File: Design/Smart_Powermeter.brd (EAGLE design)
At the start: 80 x 70 mm, 48 parts, among them J1 AUDIO_JACK_TRRSSMD_RA, J2 AUDIO_JACK_TRRSSMD_RA, J3 AUDIO_JACK_TRRSSMD_RA, J4 AUDIO_JACK_TRRSSMD_RA, J5 AUDIO_JACK_TRRSSMD_RA, J6 AUDIO_JACK_TRRSSMD_RA, J7 AUDIO_JACK_TRRSSMD_RA, J8 AUDIO_JACK_TRRSSMD_RA

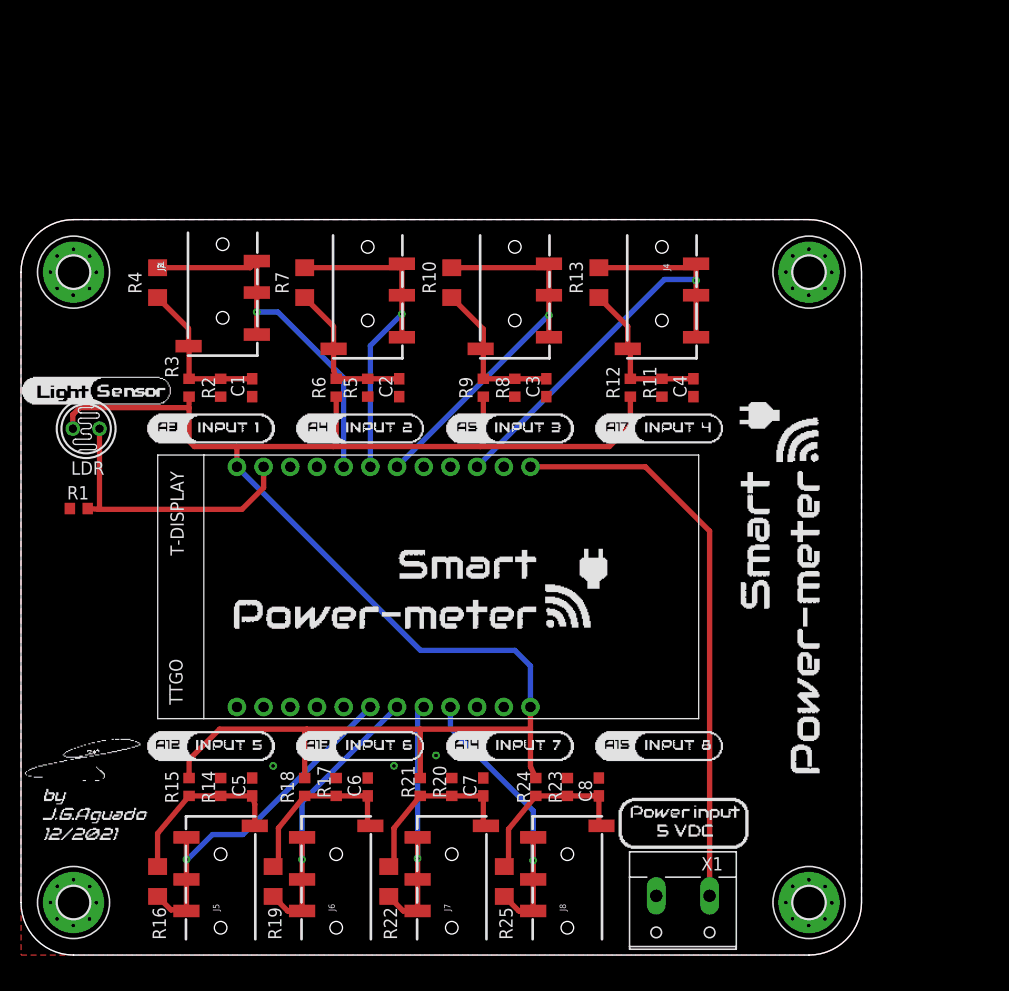
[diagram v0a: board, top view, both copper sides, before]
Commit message: Updated design files fixing Release 1 bugs
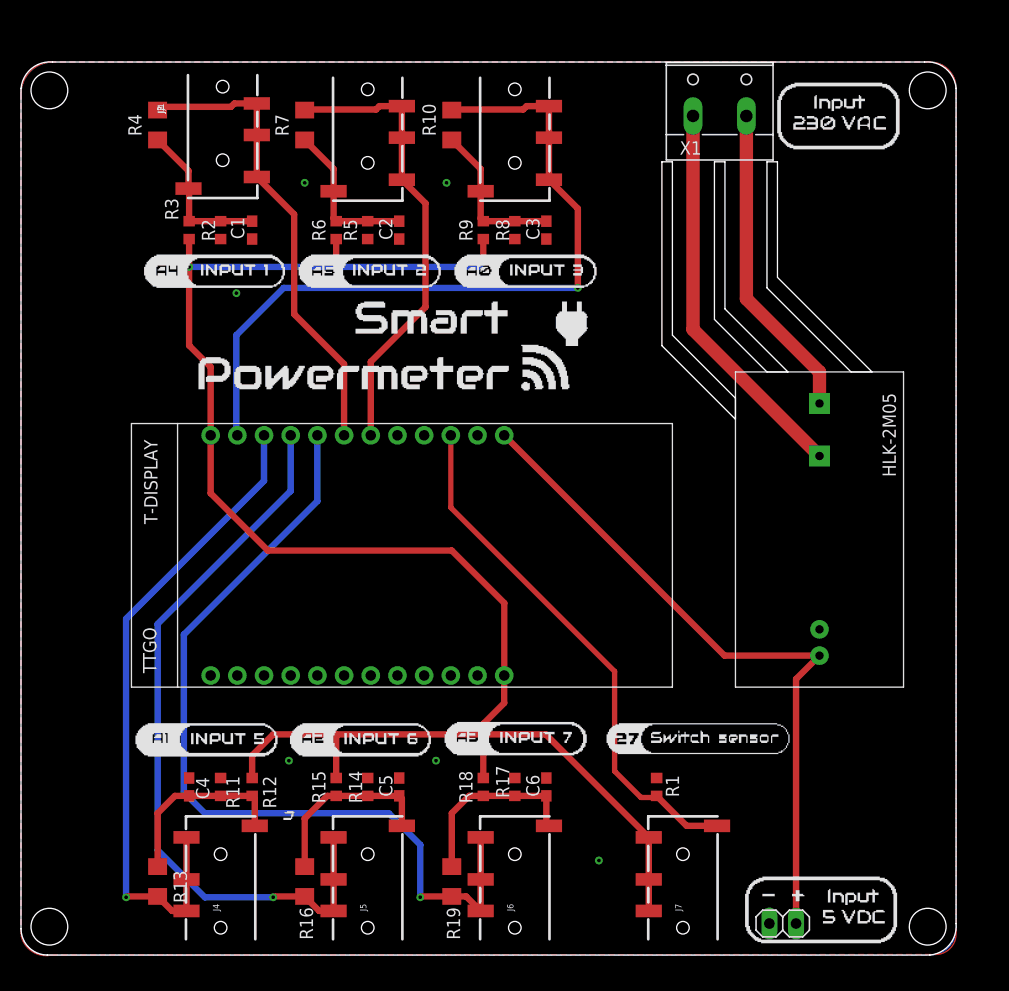
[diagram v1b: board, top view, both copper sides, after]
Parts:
- removed C7, C8: 10u, rcl:C0603
- removed H1, H2, H3, H4: MOUNT-PAD-ROUND3.0, holes:3,0-PAD
- removed J8: AUDIO_JACK_TRRSSMD_RA, SparkFun-Connectors:AUDIO_JACK_3.5MM_TRRS_SMD_RA
- removed LDR: VT20N1, photo-elements:TO46-VT200
- removed R20, R21, R23, R24: 10k, rcl:R0603
- removed R22, R25: 22, rcl:R1206
- added JP1: (no value), pinhead:1X02
- added U$2: HLK-2M05, SpaceDIY_modules:HLK-2M05
- moved J4 79.9 mm to (19.0, 1.00), turned to 90 degrees
- moved X1 75.6 mm to (66.5, 80.5), turned to 0 degrees
- moved R13 70.8 mm to (13.0, 7.00), turned to 270 degrees
- moved C4 61.2 mm to (16.0, 16.0), turned to 90 degrees
- moved R1 61.1 mm to (60.5, 16.0), turned to 270 degrees
- moved R11 56.6 mm to (19.0, 16.0), turned to 270 degrees
- moved R12 52.3 mm to (22.0, 16.0), turned to 90 degrees
- moved J7 22.0 mm to (63.0, 1.00)
- moved C6 17.0 mm to (50.0, 16.0)
- moved J6 17.0 mm to (47.0, 1.00)
- moved R17 17.0 mm to (47.0, 16.0)
- moved R18 17.0 mm to (44.0, 16.0)
- moved R19 17.0 mm to (41.0, 7.00)
- moved C1 15.0 mm to (22.0, 69.0)
- moved C2 15.0 mm to (36.0, 69.0)
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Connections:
- removed net LIGHT: LDR.2, R1.2, U$1.SVP-G36-A0
- removed net M7: J7.RING1, J7.RING2, J7.TIP, R22.2, U$1.13-G13-A14
- removed net M8: J8.RING1, J8.RING2, J8.TIP, R25.2, U$1.12-G12-A15
- removed net VG7: C7.1, J7.EARTH, R20.2, R21.1, R22.1
- removed net VG8: C8.1, J8.EARTH, R23.2, R24.1, R25.1
- new net N$1: U$2.AC1, X1.2
- new net N$2: U$2.AC2, X1.1
- new net PB: J7.EARTH, R1.2, U$1.27-G27-A17
- net 3.3V: now also J7.RING1, J7.RING2, J7.TIP; no longer LDR.1, R21.2, R24.2
- net 5V: now also JP1.2, U$2.+V0; no longer X1.1
- net GND: now also JP1.1, U$2.-V0; no longer C7.2, C8.2, H1.B3,0, H2.B3,0, H3.B3,0, H4.B3,0, R20.1, R23.1, X1.2
- net M1: now also U$1.32-G32-A4; no longer U$1.SVN-G39-A3
- net M2: now also U$1.33-G33-A5; no longer U$1.32-G32-A4
- net M3: now also U$1.SVP-G36-A0; no longer U$1.33-G33-A5
- net M4: now also U$1.37-G37; no longer U$1.27-G27-A17
- net M5: now also U$1.38-G38; no longer U$1.2-G2-A12
- net M6: now also U$1.SVN-G39-A3; no longer U$1.15-G15-A13
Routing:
- net M6: track 28.6 -> 82.2 mm
- net PB: track 0.00 -> 50.5 mm
- net N$2: track 0.00 -> 37.4 mm
- net M5: track 33.8 -> 70.9 mm
- net M3: track 36.8 -> 71.8 mm
- net N$1: track 0.00 -> 30.2 mm
- net M8: track 28.2 -> 0.00 mm, vias 1 -> 0
- net LIGHT: track 27.3 -> 0.00 mm
- net M7: track 25.0 -> 0.00 mm, vias 1 -> 0
- net M4: track 44.7 -> 62.8 mm
- net VG8: track 17.2 -> 0.00 mm
- net VG7: track 16.9 -> 0.00 mm
- net M2: track 32.2 -> 43.8 mm, vias 1 -> 0
- net 5V: track 54.3 -> 65.1 mm
- net M1: track 36.0 -> 44.7 mm, vias 1 -> 0
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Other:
- board size 80 x 70 mm -> 89 x 85 mm

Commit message: Resize dimensions to fit in the 92x87 enclosure
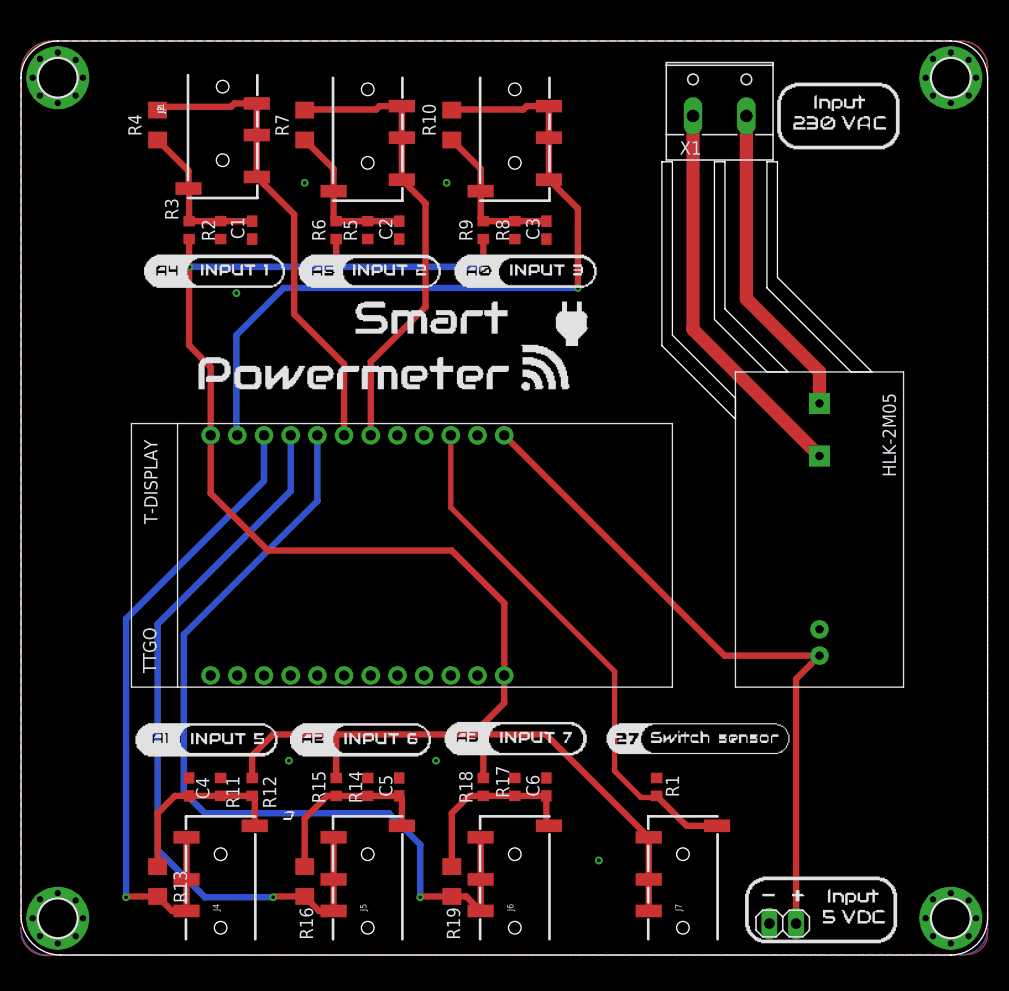
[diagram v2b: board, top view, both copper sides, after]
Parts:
- added FRAME1: (no value), SpaceDIY_symbols:92X87
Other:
- board size 89 x 85 mm -> 92 x 87 mm
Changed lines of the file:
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@@
 <setting verticaltext="up"/>
 </settings>
-<grid distance="0.1177" unitdist="mm" unit="mm" style="lines" multiple="1" display="yes" altdistance="5" altunitdist="mil" altunit="mil"/>
+<grid distance="1" unitdist="mm" unit="mm" style="lines" multiple="1" display="yes" altdistance="5" altunitdist="mil" altunit="mil"/>
 <layers>
 <layer number="1" name="Top" color="4" fill="1" visible="yes" active="yes"/>
@@
 <layer number="47" name="Measures" color="7" fill="1" visible="no" active="yes"/>
 <layer number="48" name="Document" color="7" fill="1" visible="no" active="yes"/>
-<layer number="49" name="Reference" color="7" fill="1" visible="no" active="yes"/>
+<layer number="49" name="Reference" color="7" fill="1" visible="yes" active="yes"/>
 <layer number="50" name="dxf" color="7" fill="1" visible="no" active="no"/>
 <layer number="51" name="tDocu" color="7" fill="1" visible="yes" active="yes"/>
@@
 <board>
 <plain>
-<wire x1="0" y1="2.5" x2="2.5" y2="0" width="0" layer="20" curve="90"/>
-<wire x1="2.5" y1="0" x2="86.5" y2="0" width="0" layer="20"/>
-<wire x1="86.5" y1="0" x2="89" y2="3" width="0" layer="20" curve="90"/>
-<wire x1="89" y1="3" x2="89" y2="82.5" width="0" layer="20"/>
-<wire x1="89" y1="82.5" x2="86" y2="85" width="0" layer="20" curve="90"/>
-<wire x1="86" y1="85" x2="3" y2="85" width="0" layer="20"/>
-<wire x1="3" y1="85" x2="0" y2="82.5" width="0" layer="20" curve="90"/>
-<wire x1="0" y1="82.5" x2="0" y2="2.5" width="0" layer="20"/>
 <rectangle x1="24.9691" y1="12.8547" x2="25.7097" y2="12.9605" layer="25"/>
 <rectangle x1="24.9691" y1="12.9605" x2="25.8155" y2="13.0663" layer="25"/>
@@
 <rectangle x1="25.0749" y1="13.4895" x2="26.0271" y2="13.5953" layer="25"/>
 <rectangle x1="25.2865" y1="13.5953" x2="25.9213" y2="13.7011" layer="25"/>
-<hole x="2.7" y="2.7" drill="3.5"/>
-<hole x="2.7" y="82.3" drill="3.5"/>
-<hole x="86.3" y="82.3" drill="3.5"/>
-<hole x="86.3" y="2.7" drill="3.5"/>
 <polygon width="0.6096" layer="41">
 <vertex x="60" y="85"/>
@@
 <attribute name="VALUE" x="69.96" y="-0.175" size="1.27" layer="27"/>
 </element>
+<element name="FRAME1" library="SpaceDIY_symbols" package="92X87" value="" x="0" y="0" smashed="yes"/>
 </elements>
 <signals>
@@
 <contactref element="U$1" pad="GND_2"/>
 <polygon width="0.508" layer="1">
-<vertex x="3" y="85" curve="90"/>
-<vertex x="0" y="82"/>
+<vertex x="3" y="87" curve="90"/>
+<vertex x="0" y="84"/>
 <vertex x="0" y="1.861153125" curve="90"/>
-<vertex x="2.91329375" y="0"/>
-<vertex x="87.05454375" y="0.05454375" curve="90"/>
-<vertex x="89" y="2"/>
-<vertex x="89" y="82.5" curve="90"/>
-<vertex x="86.5" y="85"/>
+<vertex x="2.916334375" y="-0.00194375"/>
+<vertex x="90.05454375" y="0.05454375" curve="90"/>
+<vertex x="92" y="2"/>
+<vertex x="92" y="84.5" curve="90"/>
+<vertex x="89.5" y="87"/>
 </polygon>
 <polygon width="0.508" layer="16">
-<vertex x="3" y="85" curve="90"/>
-<vertex x="0" y="82"/>
+<vertex x="3" y="87" curve="90"/>
+<vertex x="0" y="84"/>
 <vertex x="0" y="2.5" curve="90"/>
 <vertex x="2.5" y="0"/>
-<vertex x="86.5" y="0" curve="90"/>
-<vertex x="89" y="2.5"/>
-<vertex x="89" y="82.5" curve="90"/>
-<vertex x="86.5" y="85"/>
+<vertex x="89.5" y="0" curve="90"/>
+<vertex x="92" y="2.5"/>
+<vertex x="92" y="84.5" curve="90"/>
+<vertex x="89.5" y="87"/>
 </polygon>
 <contactref element="U$2" pad="-V0"/>

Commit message: Added design files of V2
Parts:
- removed JP1: (no value), pinhead:1X02
- added C10, C12, C16, C20, C8: 10uF, rcl:C0603
- added C11, C15, C21: 0.1uF, rcl:C0603
- added C13, C14, C17, C18, C19, C25, C27, C28, C9: 1uF, rcl:C0603
- added C26, C7: 4.7uF, rcl:C0603
- added D1, D2, D3: SS14, SpaceDIY_semiconductors:SMA-DIODE
- added DISP1: DISP_LCD_GENERIC_SPI_1.69_WRAPUNDER, adafruit_display:TFT_1.69IN_240X280_12P
- added IC1: AMS1117-3.3, SparkFun-IC-Power:SOT223
- added IC3: ESP32-S2-MINI-1-N4R2, SpaceDIY_modules:ESP32S2MINI1N4R2
- added IC5: BMP280, SamacSys_Parts:8-PIN-METAL-LID-LGA
- added J8: USB-C, SparkFun-Connectors:USB-C-16P-4LAYER-ISOLATED
- added L3: 10uH, microbuilder:INDUCTOR_4X4MM_NR401
- added Q1: IRLML0100, Parts:SOT23-3
- added Q2: 2N7002, SparkFun-DiscreteSemi:SOT23-3
- added R20, R21, R22, R26, R28, R29: 10k, rcl:R0603
- added R23, R24: 4.7k, rcl:R0603
- added R25: 10K, rcl:R0603
- added R27: 10, rcl:R0603
- added R36, R37: 5.1k, rcl:R0603
- added S1: Flash, SpaceDIY_electromechanical:TACTILE_SWITCH_SMD_5.2MM
- added S2: Reset, SpaceDIY_electromechanical:TACTILE_SWITCH_SMD_5.2MM
- added SJ1, SJ2: SOLDERJUMPERROUND, SparkFun-Retired:SJ_ROUND
- H1: value (none) -> 92X84
- J7: value AUDIO_JACK_TRRSSMD_RA -> (none); device SparkFun-Connectors:AUDIO_JACK_3.5MM_TRRS_SMD_RA -> SparkFun-Connectors:1X04
- R1: value 10k -> 0.47
- U$1: value TTGO-T-DISPLAYFRAME -> E-PAPER-FPC_2; device TTGO-TDisplay:TTGO-T-DISPLAY-OL -> SpaceDIY_connectors:FPC-05FB-24PH20
- moved X1 75.2 mm to (72.5, 5.50), turned to 180 degrees
- moved R1 61.3 mm to (20.0, 62.0), turned to 180 degrees
- moved U$1 51.2 mm to (17.0, 50.0), turned to 270 degrees
- moved J7 39.7 mm to (89.0, 31.0)
- moved U$2 33.7 mm to (87.5, 28.0), turned to 180 degrees
- moved C1 0.50 mm to (22.0, 69.5)
- moved C2 0.50 mm to (36.0, 69.5)
- moved C3 0.50 mm to (50.0, 69.5)
- moved R2 0.50 mm to (19.0, 69.5)
- moved R3 0.50 mm to (16.0, 69.5)
- moved R5 0.50 mm to (33.0, 69.5)
- moved R6 0.50 mm to (30.0, 69.5)
- moved R8 0.50 mm to (47.0, 69.5)
- moved R9 0.50 mm to (44.0, 69.5)
- renumbered FRAME1 to H1
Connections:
- removed net M6: J6.RING1, J6.RING2, J6.TIP, R19.2, U$1.SVN-G39-A3
- removed net PB: J7.EARTH, R1.2, U$1.27-G27-A17
- removed net VG6: C6.1, J6.EARTH, R17.2, R18.1, R19.1
- new net BK_LIGHT: Q2.1, R26.1
- new net CC3: J8.B5, R36.2
- new net CC4: J8.A5, R37.2
- new net D+: IC3.24, J8.A6, J8.B6
- new net D-: IC3.23, J8.A7, J8.B7
- new net GDR: Q1.1, R20.1, U$1.23
- new net IO0: IC3.4, S1.3
- new net LEDK: DISP1.2, R27.2
- new net M0: IC3.5, J1.RING1, J1.RING2, J1.TIP, R4.2
- new net N$10: IC5.5, R23.2
- new net N$11: C9.2, U$1.20
- new net N$12: C13.2, U$1.7
- new net N$13: C14.2, U$1.5
- new net N$14: C17.2, U$1.3
- new net N$15: C18.2, U$1.1
- new net N$16: C26.2, D2.A, D3.C
- new net N$17: C26.1, D1.A, L3.P$1, Q1.3
- new net N$3: IC5.2, R24.2
- new net N$31: C27.2, U$1.21
- new net N$32: C28.2, U$1.6
- new net N$4: Q2.3, R27.1
- new net N$5: R28.1, SJ1.2
- new net N$6: R29.1, SJ2.2
- new net RESE: Q1.2, R1.1, U$1.22
- new net RST: IC3.45, R25.1, S2.3
- new net RX: IC3.40, J7.4
- new net SCL: IC3.29, IC5.4, R21.2
- new net SDA: IC3.28, IC5.3, R22.2
- new net SPI_BUSY: IC3.18, U$1.16
- new net SPI_CLK: DISP1.9, IC3.16, U$1.12
- new net SPI_CS: DISP1.8, IC3.14, SJ2.1, U$1.13
- new net SPI_MISO: DISP1.7, IC3.17, U$1.14
- new net SPI_MOSI: DISP1.10, IC3.15, U$1.11
- new net SPI_RST: DISP1.11, IC3.19, SJ1.1, U$1.15
- new net TX: IC3.39, J7.3
- new net VG0: C1.1, J1.EARTH, R2.2, R3.1, R4.1
- new net VGH: C19.1, D1.C, U$1.4
- new net VGL: C25.1, D3.A, U$1.2
- net 3.3V: now also C10.1, C11.1, C12.1, C15.1, C16.1, C20.1, C21.1, C7.1, DISP1.3, DISP1.4, IC1.2, IC3.3, IC5.6, IC5.8, L3.P$2, R21.1, R22.1, R23.1, R24.1, R25.2, R26.2, R28.2, R29.2, U$1.10, U$1.9; no longer J7.RING1, J7.RING2, J7.TIP, U$1.3V3_0, U$1.3V3_1
- net 5V: now also C8.1, IC1.3, J7.1, J8.VBUS1, J8.VBUS2; no longer JP1.2, U$1.5V
- net GND: now also C10.2, C11.2, C12.2, C13.1, C14.1, C15.2, C16.2, C17.1, C18.1, C19.2, C20.2, C21.2, C25.2, C27.1, C28.1, C7.2, C8.2, C9.1, D2.C, DISP1.1, DISP1.12, DISP1.5, DISP1.6, H1.B3,1, H1.B3,2, H1.B3,3, H1.B3,6, H1.P$1, H1.P$10, H1.P$11, H1.P$12, H1.P$13, H1.P$14, H1.P$15, H1.P$16, H1.P$17, H1.P$18, H1.P$19, H1.P$2, H1.P$20, H1.P$21, H1.P$22, H1.P$23, H1.P$24, H1.P$25, H1.P$26, H1.P$27, H1.P$28, H1.P$29, H1.P$3, H1.P$30, H1.P$31, H1.P$32, H1.P$4, H1.P$5, H1.P$6, H1.P$7, H1.P$8, H1.P$9, IC1.1, IC3.1, IC3.2, IC3.30, IC3.42, IC3.43, IC3.46, IC3.47, IC3.48, IC3.49, IC3.50, IC3.51, IC3.52, IC3.53, IC3.54, IC3.55, IC3.56, IC3.57, IC3.58, IC3.59, IC3.60, IC3.61, IC3.62, IC3.63, IC3.64, IC3.65, IC3.66, IC3.67, IC3.68, IC3.69, IC3.70, IC3.71, IC3.72, IC3.73, IC5.1, IC5.7, J7.2, J8.GND, J8.GND2, Q2.2, R1.2, R20.2, R36.1, R37.1, S1.1, S2.1, U$1.17, U$1.8; no longer JP1.1, R1.1, U$1.GND_0, U$1.GND_1, U$1.GND_2, U$1.GND_3, U$1.GND_4
- net M1: now also IC3.6, J2.RING1, J2.RING2, J2.TIP, R7.2; no longer J1.RING1, J1.RING2, J1.TIP, R4.2, U$1.32-G32-A4
- net M2: now also IC3.7, J3.RING1, J3.RING2, J3.TIP, R10.2; no longer J2.RING1, J2.RING2, J2.TIP, R7.2, U$1.33-G33-A5
- net M3: now also IC3.8, J4.RING1, J4.RING2, J4.TIP, R13.2; no longer J3.RING1, J3.RING2, J3.TIP, R10.2, U$1.SVP-G36-A0
- net M4: now also IC3.9, J5.RING1, J5.RING2, J5.TIP, R16.2; no longer J4.RING1, J4.RING2, J4.TIP, R13.2, U$1.37-G37
- net M5: now also IC3.10, J6.RING1, J6.RING2, J6.TIP, R19.2; no longer J5.RING1, J5.RING2, J5.TIP, R16.2, U$1.38-G38
- net N$1: now also U$2.AC2; no longer U$2.AC1
- net N$2: now also U$2.AC1; no longer U$2.AC2
- net VG1: now also C2.1, J2.EARTH, R5.2, R6.1, R7.1; no longer C1.1, J1.EARTH, R2.2, R3.1, R4.1
- net VG2: now also C3.1, J3.EARTH, R10.1, R8.2, R9.1; no longer C2.1, J2.EARTH, R5.2, R6.1, R7.1
- net VG3: now also C4.1, J4.EARTH, R11.2, R12.1, R13.1; no longer C3.1, J3.EARTH, R10.1, R8.2, R9.1
- net VG4: now also C5.1, J5.EARTH, R14.2, R15.1, R16.1; no longer C4.1, J4.EARTH, R11.2, R12.1, R13.1
- net VG5: now also C6.1, J6.EARTH, R17.2, R18.1, R19.1; no longer C5.1, J5.EARTH, R14.2, R15.1, R16.1
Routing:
- net 3.3V: track 164.0 -> 265.6 mm, vias 3 -> 6
- net SDA: track 0.00 -> 91.8 mm, vias 0 -> 4
- net SCL: track 0.00 -> 88.0 mm, vias 0 -> 4
- net M0: track 0.00 -> 85.4 mm
- net M6: track 82.2 -> 0.00 mm, vias 1 -> 0
- net SPI_CS: track 0.00 -> 78.7 mm, vias 0 -> 6
- net SPI_MOSI: track 0.00 -> 73.1 mm, vias 0 -> 5
- net SPI_MISO: track 0.00 -> 72.3 mm, vias 0 -> 3
- net SPI_CLK: track 0.00 -> 69.1 mm, vias 0 -> 5
- net SPI_RST: track 0.00 -> 66.5 mm, vias 0 -> 4
- net 5V: track 65.1 -> 124.5 mm, vias 0 -> 2
- net SPI_BUSY: track 0.00 -> 56.5 mm, vias 0 -> 2
- net M3: track 71.8 -> 128.0 mm, vias 1 -> 4
- net M4: track 62.8 -> 117.5 mm, vias 1 -> 4
- net RST: track 0.00 -> 53.9 mm, vias 0 -> 2
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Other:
- board text added: "JLCJLCJLCJLC"

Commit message: Updated design files
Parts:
- removed C15, C21: 0.1uF, rcl:C0603
- removed C16, C20: 10uF, rcl:C0603
- removed DISP1: DISP_LCD_GENERIC_SPI_1.69_WRAPUNDER, adafruit_display:TFT_1.69IN_240X280_12P
- removed IC5: BMP280, SamacSys_Parts:8-PIN-METAL-LID-LGA
- removed Q2: 2N7002, SparkFun-DiscreteSemi:SOT23-3
- removed R21, R22, R26, R28, R29: 10k, rcl:R0603
- removed R23, R24: 4.7k, rcl:R0603
- removed R27: 10, rcl:R0603
- removed SJ1, SJ2: SOLDERJUMPERROUND, SparkFun-Retired:SJ_ROUND
- added J9: (no value), SparkFun-Connectors:1X04
- moved IC1 5.10 mm to (82.0, 74.0)
- moved C8 5.00 mm to (75.0, 72.0)
- moved C10 3.00 mm to (75.0, 74.0)
- moved J2 2.50 mm to (33.0, 86.5)
- moved J3 2.50 mm to (47.0, 86.5)
- moved C1 2.40 mm to (22.1, 71.9)
- moved C2 2.40 mm to (36.1, 71.9)
- moved C3 2.40 mm to (50.1, 71.9)
- moved R2 2.40 mm to (19.1, 71.9)
- moved R3 2.40 mm to (16.1, 71.9)
- moved R5 2.40 mm to (33.1, 71.9)
- moved R6 2.40 mm to (30.1, 71.9)
- moved R8 2.40 mm to (47.1, 71.9)
- moved R9 2.40 mm to (44.1, 71.9)
- moved J1 2.25 mm to (19.2, 86.5)
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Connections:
- removed net BK_LIGHT: Q2.1, R26.1
- removed net LEDK: DISP1.2, R27.2
- removed net M0: IC3.5, J1.RING1, J1.RING2, J1.TIP, R4.2
- removed net N$10: IC5.5, R23.2
- removed net N$3: IC5.2, R24.2
- removed net N$4: Q2.3, R27.1
- removed net N$5: R28.1, SJ1.2
- removed net N$6: R29.1, SJ2.2
- new net M6: IC3.10, J6.RING1, J6.RING2, J6.TIP, R19.2
- net 3.3V: now also J9.2; no longer C15.1, C16.1, C20.1, C21.1, DISP1.3, DISP1.4, IC5.6, IC5.8, R21.1, R22.1, R23.1, R24.1, R26.2, R28.2, R29.2
- net GND: now also J9.1; no longer C15.2, C16.2, C20.2, C21.2, DISP1.1, DISP1.12, DISP1.5, DISP1.6, IC5.1, IC5.7, Q2.2
- net M1: now also IC3.5, J1.RING1, J1.RING2, J1.TIP, R4.2; no longer IC3.6, J2.RING1, J2.RING2, J2.TIP, R7.2
- net M2: now also IC3.6, J2.RING1, J2.RING2, J2.TIP, R7.2; no longer IC3.7, J3.RING1, J3.RING2, J3.TIP, R10.2
- net M3: now also IC3.7, J3.RING1, J3.RING2, J3.TIP, R10.2; no longer IC3.8, J4.RING1, J4.RING2, J4.TIP, R13.2
- net M4: now also IC3.8, J4.RING1, J4.RING2, J4.TIP, R13.2; no longer IC3.9, J5.RING1, J5.RING2, J5.TIP, R16.2
- net M5: now also IC3.9, J5.RING1, J5.RING2, J5.TIP, R16.2; no longer IC3.10, J6.RING1, J6.RING2, J6.TIP, R19.2
- net SCL: now also J9.4; no longer IC5.4, R21.2
- net SDA: now also J9.3; no longer IC5.3, R22.2
- net SPI_CLK: no longer DISP1.9
- net SPI_CS: no longer DISP1.8, SJ2.1
- net SPI_MISO: no longer DISP1.7
- net SPI_MOSI: no longer DISP1.10
- net SPI_RST: no longer DISP1.11, SJ1.1
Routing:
- net M6: track 0.00 -> 104.3 mm, vias 0 -> 4
- net M0: track 85.4 -> 0.00 mm
- net M3: track 128.0 -> 64.1 mm, vias 4 -> 2
- net 3.3V: track 265.6 -> 206.4 mm, vias 6 -> 5
- net SDA: track 91.8 -> 36.0 mm, vias 4 -> 1
- net SCL: track 88.0 -> 34.7 mm, vias 4 -> 1
- net M2: track 62.0 -> 77.8 mm
- net M5: track 103.7 -> 118.0 mm
- net M1: track 75.7 -> 87.6 mm, vias 2 -> 0
- net M4: track 117.5 -> 129.1 mm
- net SPI_MISO: track 72.3 -> 64.4 mm, vias 3 -> 2
- net SPI_CS: track 78.7 -> 72.0 mm, vias 6 -> 4
- net SPI_RST: track 66.5 -> 60.2 mm, vias 4 -> 3
- net SPI_MOSI: track 73.1 -> 67.0 mm, vias 5 -> 4
- net LEDK: track 4.41 -> 0.00 mm
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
